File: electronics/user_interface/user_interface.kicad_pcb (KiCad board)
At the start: 2 copper layers, 80 x 80 mm, 91 parts, among them J1 Conn_01x06, J2 Conn_02x05_Odd_Even, SW1 ALPS_EC11E18244A5, U1 PCF8574, U2 PCF8574

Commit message: updated versionnumber
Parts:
- N2: value V20200605 -> V20200703

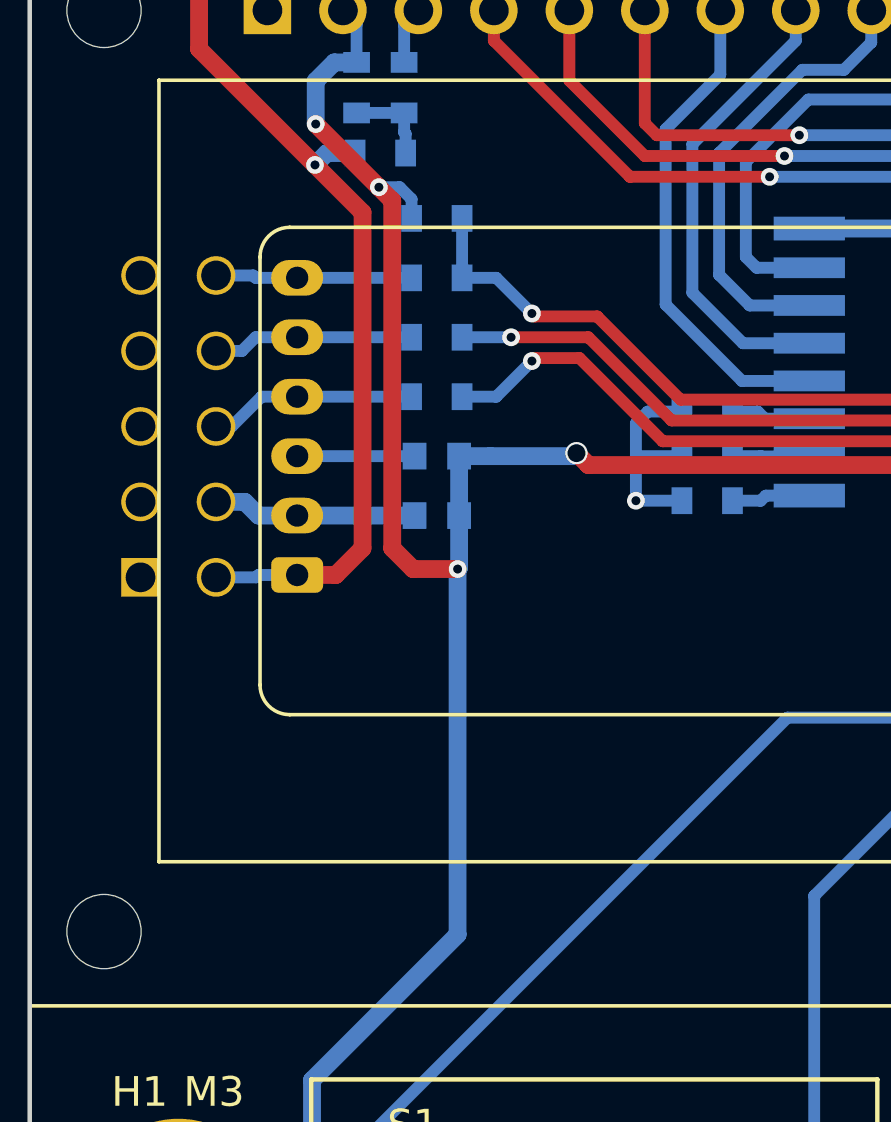
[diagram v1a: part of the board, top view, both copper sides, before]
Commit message: WIP adding labels to connectors
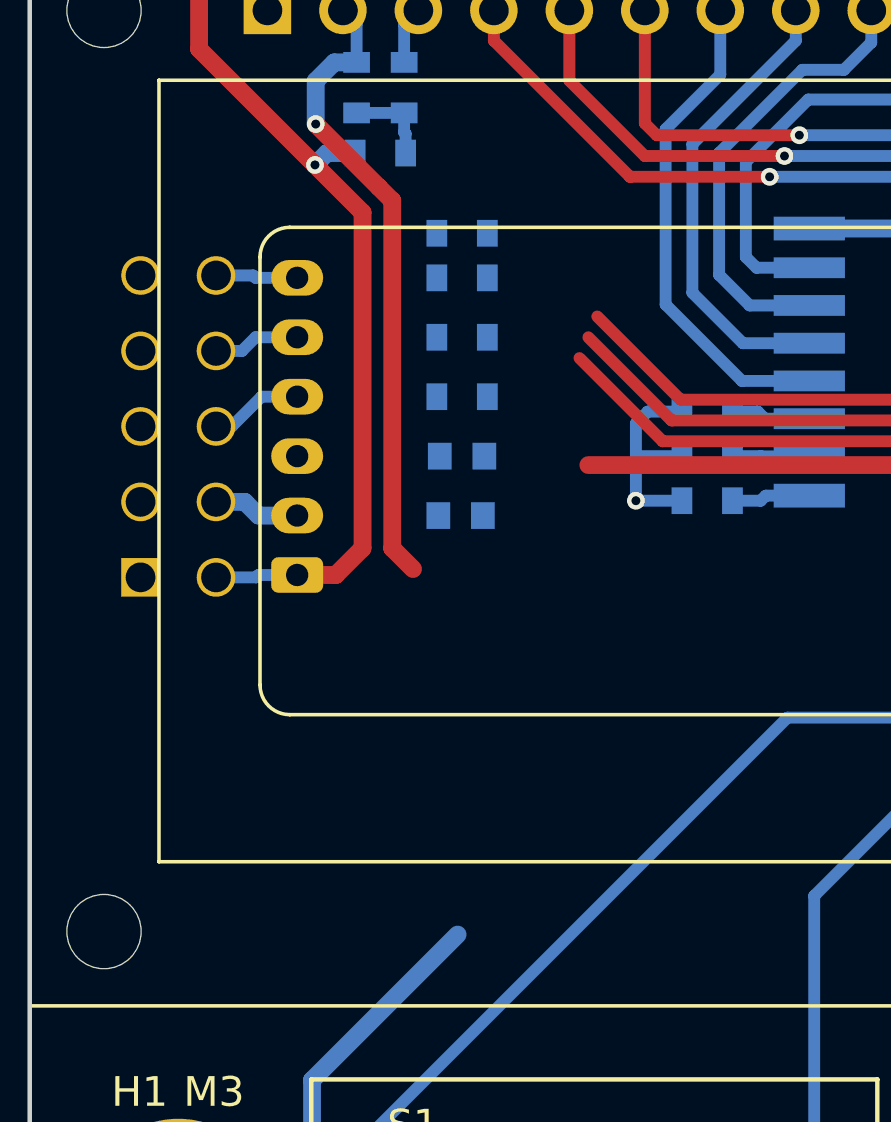
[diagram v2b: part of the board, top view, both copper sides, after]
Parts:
- moved R1 0.99 mm to (124.5, 82.0)
- moved C1 0.85 mm to (124.5, 89.5)
- moved R2 0.85 mm to (124.5, 87.5)
- moved R3 0.85 mm to (124.5, 85.5)
- moved R4 0.85 mm to (124.5, 83.5)
- moved FB1 0.80 mm to (124.5, 91.5)
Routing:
- net /VDD: track 400.8 -> 376.7 mm, vias 7 -> 4
- net /!INT: track 51.6 -> 44.5 mm, vias 3 -> 2
- net /SDA: track 46.3 -> 41.9 mm, vias 3 -> 2
- net /SCL: track 42.7 -> 38.5 mm, vias 3 -> 2
- net /VSS: track 81.0 -> 77.1 mm
- net /VDD_RAW: track 6.87 -> 2.92 mm
- net /SDA_RAW: track 6.99 -> 3.14 mm
- net /SCL_RAW: track 6.77 -> 2.92 mm
- net /!INT_RAW: track 6.61 -> 2.76 mm
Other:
- board text added: "INT"
- board text added: "SCL"
- board text added: "SDA"
- board text added: "VDD"
- board text added: "VDD_BACKLIGHT"
- board text added: "VSS"
